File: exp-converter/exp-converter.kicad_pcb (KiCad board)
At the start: 2 copper layers, 51.3 x 22 mm, 28 parts, among them J1 AudioJack2_Ground, J2 AudioJack2_Ground, J3 Conn_02x08_Odd_Even, J4 AudioJack2_Ground, J5 AudioJack2_Ground, Q1 BC548, Q2 BC548, U1 LM358, U2 LM358, U3 LM3046N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

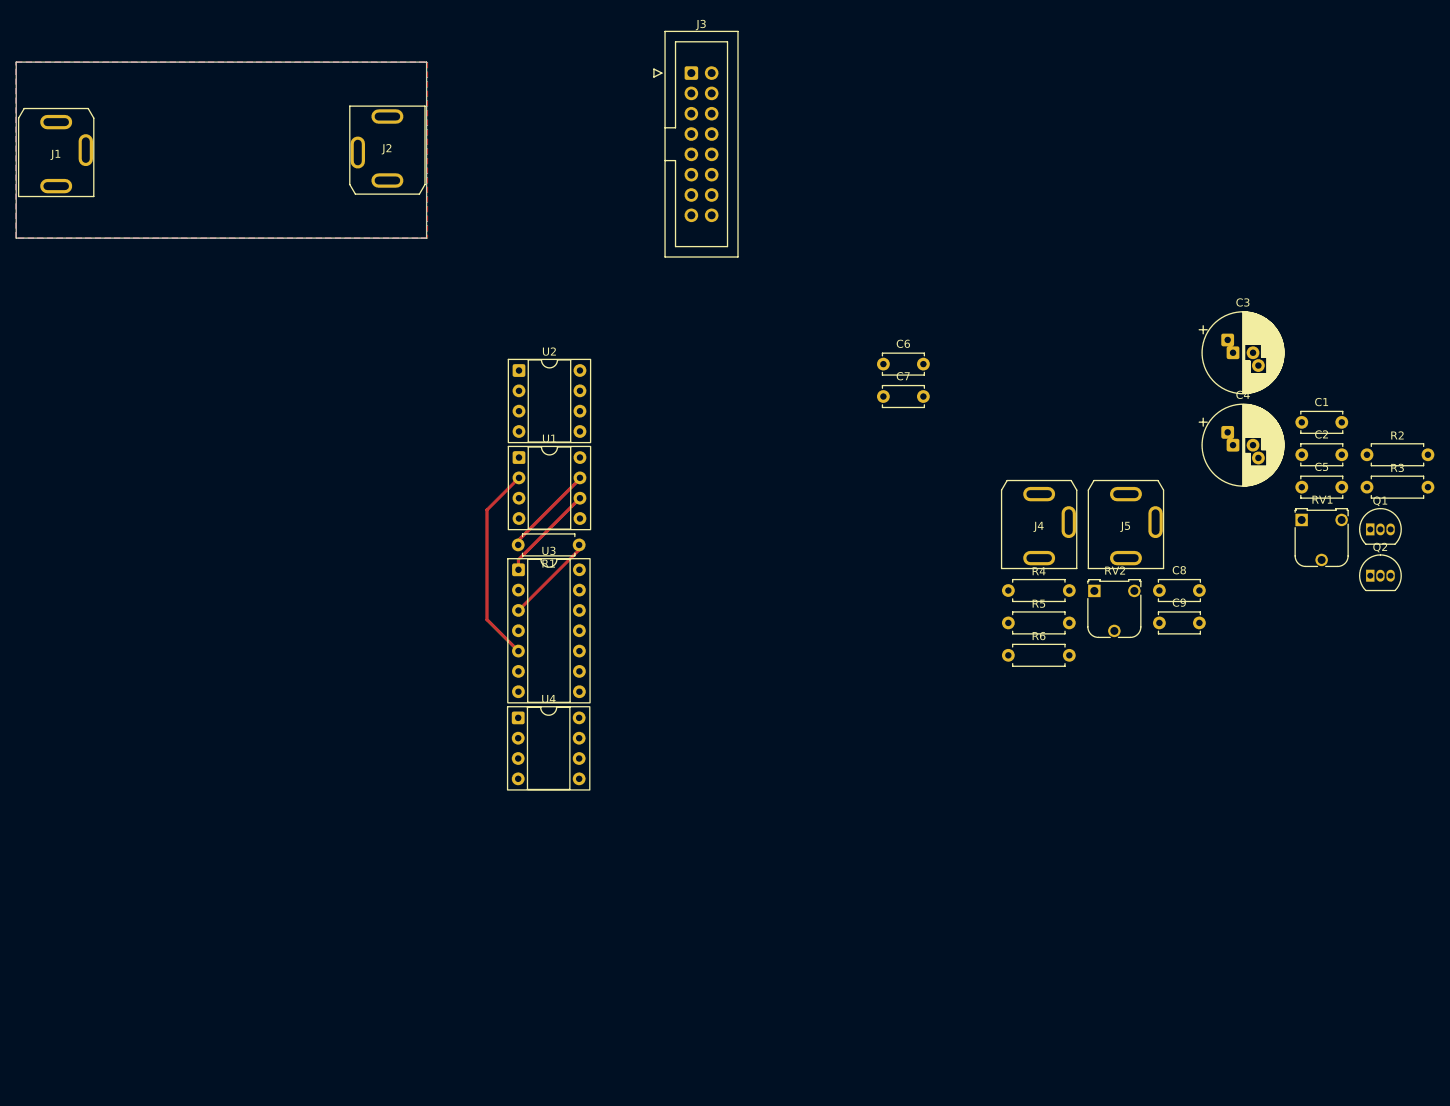
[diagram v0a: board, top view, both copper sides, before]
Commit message: Exp. converter parts placed
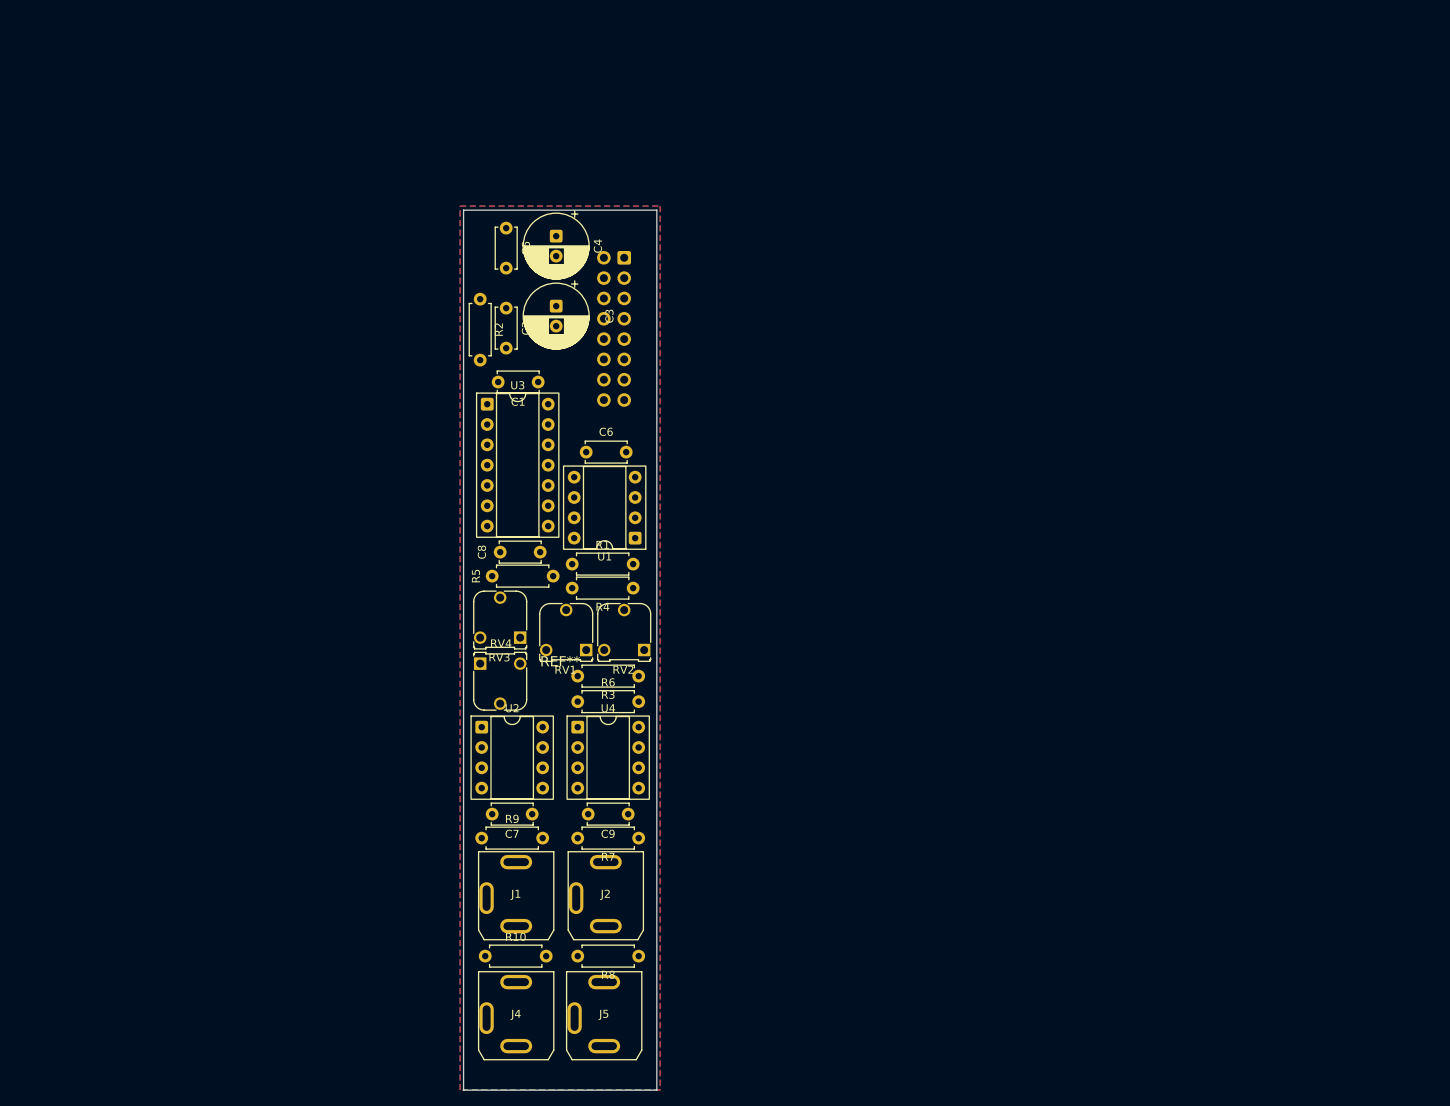
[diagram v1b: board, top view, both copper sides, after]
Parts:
- removed Q1, Q2: BC548, Package_TO_SOT_THT:TO-92_Inline
- added R10: 100k, 00_exp-converter:R_Axial_DIN0207_L6.3mm_D2.5mm_P7.62mm_Horizontal, F.Cu at (90.6, 141.8)
- added R7: 1k, 00_exp-converter:R_Axial_DIN0207_L6.3mm_D2.5mm_P7.62mm_Horizontal, F.Cu at (109.8, 127.0)
- added R8: 1k, 00_exp-converter:R_Axial_DIN0207_L6.3mm_D2.5mm_P7.62mm_Horizontal, F.Cu at (109.8, 141.8)
- added R9: 100k, 00_exp-converter:R_Axial_DIN0207_L6.3mm_D2.5mm_P7.62mm_Horizontal, F.Cu at (90.2, 127.0)
- added REF**: Eurorack_Panel_3U_2HP, Eurorack_Panel_3U_2HP, F.Cu at (100.0, 103.5)
- added RV3: 10k, Potentiometer_THT:Potentiometer_Runtron_RM-065_Vertical, F.Cu at (95.0, 101.9)
- added RV4: 10k, Potentiometer_THT:Potentiometer_Runtron_RM-065_Vertical, F.Cu at (90.0, 105.2)
- C3, C4: footprint Capacitor_THT:CP_Radial_D10.0mm_P2.50mm_P5.00mm -> Capacitor_THT:CP_Radial_D8.0mm_P2.50mm
- J3: moved to B.Cu
- moved R2 112.5 mm to (90.0, 59.6), turned to -90 degrees
- moved J1 109.8 mm to (94.5, 134.5), turned to 180 degrees
- moved C5 104.6 mm to (93.2, 50.8), turned to -90 degrees
- moved C2 101.1 mm to (93.2, 60.8), turned to -90 degrees
- moved J2 97.1 mm to (105.7, 134.5)
- moved C1 95.6 mm to (97.2, 70.0), turned to 180 degrees
- moved R3 94.1 mm to (109.8, 106.8), turned to 180 degrees
- moved RV1 90.9 mm to (103.2, 103.5), turned to 180 degrees
- moved J4 90.1 mm to (94.5, 149.5), turned to 180 degrees
- moved J5 90.0 mm to (105.5, 149.5), turned to 180 degrees
- moved C4 88.5 mm to (99.5, 51.8), turned to -90 degrees
- moved C3 84.8 mm to (99.5, 60.5), turned to -90 degrees
- moved C8 82.5 mm to (92.5, 91.2)
- moved C9 70.6 mm to (108.5, 124.0), turned to 180 degrees
- moved C7 68.2 mm to (96.5, 124.0), turned to 180 degrees
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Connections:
- C1 pad 2: Net-(U1B--) -> Net-(U1A--)
- C8 pad 2: Net-(U3B-C) -> Net-(U1B--)
- J1 pad T: Net-(U2A-+) -> Net-(J1-PadT)
- J4 pad T: Net-(U2B-+) -> Net-(J4-PadT)
- R2 pad 2: Net-(U1B--) -> Net-(U1A--)
- R3 pad 1: Net-(U1A--) -> Net-(U4A--)
- R4 pad 2: Net-(U3B-C) -> Net-(U1B--)
- RV1 pad 3: Net-(J2-PadT) -> Net-(R7-Pad1)
- RV2 pad 3: Net-(J5-PadT) -> Net-(R8-Pad1)
- U1 pad 1: Net-(J2-PadT) -> Net-(C1-Pad1)
- U1 pad 7: Net-(C1-Pad1) -> Net-(C8-Pad1)
- U2 pad 1: Net-(U2A--) -> Net-(RV3-Pad2)
- U2 pad 3: Net-(U2A-+) -> GND
- U2 pad 5: Net-(U2B-+) -> GND
- U2 pad 7: Net-(U2B--) -> Net-(U3B-B)
- U3 pad 1: Net-(U1B--) -> Net-(U1A--)
- U3 pad 2: Net-(U2A--) -> Net-(RV3-Pad2)
- U3 pad 5: Net-(U1A--) -> Net-(U4A--)
- U3 pad 6: Net-(U2B--) -> Net-(U3B-B)
- U3 pad 8: Net-(U3B-C) -> Net-(U1B--)
- U4 pad 1: Net-(C8-Pad1) -> Net-(R7-Pad1)
- U4 pad 2: Net-(U3B-C) -> Net-(U4A--)
- U4 pad 4: VCC -> VEE
- U4 pad 7: Net-(J5-PadT) -> Net-(R8-Pad1)
- U4 pad 8: VEE -> VCC
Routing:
- net Net-(U1A--): track 24.9 -> 0.00 mm
- net Net-(U1B--): track 12.1 -> 0.00 mm
- net Net-(C1-Pad1): track 11.6 -> 0.00 mm
- net Net-(U3A-E): track 11.3 -> 0.00 mm
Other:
- board size 51.3 x 22 mm -> 24.2 x 110 mm

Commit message: Nearly finished exp converter PCB.
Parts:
- moved C1 0.52 mm to (97.6, 69.6)
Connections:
- U3 pad 12: unconnected-(U3D-B-Pad12) -> GND
- U3 pad 13: unconnected-(U3D-E-Pad13) -> GND
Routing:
- net VCC: track 0.00 -> 126.1 mm, vias 0 -> 2
- net VEE: track 0.00 -> 113.1 mm
- net Net-(U4A--): track 0.00 -> 49.6 mm, vias 0 -> 3
- net Net-(RV3-Pad2): track 0.00 -> 44.4 mm
- net Net-(R8-Pad1): track 0.00 -> 44.0 mm
- net Net-(U3C-C): track 0.00 -> 43.2 mm, vias 0 -> 1
- net Net-(U2B--): track 0.00 -> 41.4 mm
- net Net-(U3B-B): track 0.00 -> 38.5 mm
- net Net-(U1A--): track 0.00 -> 36.6 mm
- net Net-(C1-Pad1): track 0.00 -> 32.9 mm
- net Net-(U2A--): track 0.00 -> 31.5 mm
- net Net-(R7-Pad1): track 0.00 -> 29.4 mm
- net Net-(U3B-E): track 0.00 -> 22.6 mm
- net Net-(U3A-E): track 0.00 -> 21.2 mm, vias 0 -> 1
- net Net-(U1B--): track 0.00 -> 14.9 mm
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
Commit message: Linear VCA mismatched TL072 power supply fixed.
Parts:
- moved J3 17.9 mm to (105.4, 72.1), turned to 0 degrees
- moved C4 10.5 mm to (99.3, 62.3)
- moved C5 10.5 mm to (93.1, 61.3)
- moved C3 8.58 mm to (99.3, 51.9)
- moved C2 8.58 mm to (93.2, 52.2)
- moved R2 8.58 mm to (90.0, 51.1)
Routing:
- net VEE: track 113.1 -> 95.5 mm
- net VCC: track 126.1 -> 139.1 mm
- net Net-(U1A--): track 36.6 -> 45.2 mm
